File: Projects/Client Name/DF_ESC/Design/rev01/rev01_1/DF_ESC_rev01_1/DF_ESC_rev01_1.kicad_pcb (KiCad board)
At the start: 2 copper layers, 100 x 75 mm, 186 parts, among them J1 XT60PW-M, J2 HX25003-8AWB, J3 S6B-XH-SM4-TB(LF)(SN), J4 XH-3AWB, J5 7461084, J6 7461084, J7 7461084, J8 USB_C_Receptacle_USB2.0, Q1 HSBA15810C, Q2 HSBA15810C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

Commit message: Update 20240416
Lesson 16 finished
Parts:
- added R64: 2k2, Resistor_SMD:R_0603_1608Metric_Pad0.98x0.95mm_HandSolder, F.Cu at (210.7, 131.1)
- C39, C42, C46: moved to B.Cu
- C41, C43, C45: footprint Capacitor_SMD:C_0603_1608Metric_Pad1.08x0.95mm_HandSolder -> Capacitor_SMD:C_1210_3225Metric
- D7: footprint PESD3V3U1UA:SOD-323_L1.7-W1.3-LS2.5-RD -> Diode_SMD:D_SOD-323_HandSoldering
- D9: footprint Diode_SMD:D_SOD-323 -> Diode_SMD:D_SOD-323_HandSoldering
- moved TH1 105.4 mm to (199.1, 156.3)
- moved R1 103.7 mm to (199.1, 157.9), turned to 180 degrees
- moved C3 100.2 mm to (201.7, 157.1), turned to 90 degrees
- moved C23 35.8 mm to (206.7, 106.3), turned to 90 degrees
- moved R20 35.2 mm to (274.4, 129.4), turned to 180 degrees
- moved D12 34.5 mm to (239.9, 167.4), turned to 90 degrees
- moved R13 33.4 mm to (205.1, 106.3), turned to 90 degrees
- moved D11 32.5 mm to (237.3, 167.4), turned to 90 degrees
- moved R21 31.7 mm to (274.5, 130.9), turned to 180 degrees
- moved R58 31.1 mm to (223.4, 128.9)
- moved R59 31.1 mm to (224.9, 128.9)
- moved R24 30.8 mm to (274.4, 159.3), turned to 180 degrees
- moved R25 28.7 mm to (274.4, 160.8), turned to 180 degrees
- moved R22 27.7 mm to (274.4, 144.3), turned to 180 degrees
- moved R11 27.1 mm to (239.9, 163.1), turned to -90 degrees
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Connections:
- C57 pad 1: +5V -> +3V3
- C58 pad 1: +5V -> +3V3
- C59 pad 1: +5V -> +3V3
- C60 pad 1: +5V -> +3V3
- R45 pad 1: +5V -> +3V3
- R46 pad 1: +5V -> +3V3
- R47 pad 1: +5V -> +3V3
- R48 pad 1: +5V -> +3V3
- SW1 pad 1: GND -> Net-(R64-Pad1)
- U6 pad 1: /[7] - CAN/C_CAN_P -> /[7] - CAN/C_CAN_N
- U6 pad 2: /[7] - CAN/C_CAN_N -> /[7] - CAN/C_CAN_P
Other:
- copper layers 2 -> 4

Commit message: update 2024-04-18
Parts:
- moved R28 12.5 mm to (251.9, 150.1), turned to 0 degrees
- moved C49 11.0 mm to (249.4, 153.4), turned to 90 degrees
- moved C48 10.6 mm to (249.2, 149.2), turned to 90 degrees
- moved R34 9.13 mm to (252.0, 154.2), turned to 0 degrees
- moved R29 8.34 mm to (251.9, 148.3), turned to 0 degrees
- moved R58 7.84 mm to (229.2, 134.1)
- moved R35 5.99 mm to (252.0, 152.4), turned to 0 degrees
- moved R59 5.81 mm to (227.4, 134.1)
- moved C33 5.06 mm to (242.2, 155.7)
- moved C35 5.06 mm to (243.7, 155.7)
- moved C32 5.04 mm to (245.3, 155.7)
- moved C11 4.64 mm to (223.4, 133.6)
- moved C24 4.58 mm to (234.1, 150.8)
- moved C27 4.58 mm to (234.1, 152.3)
- moved C31 4.58 mm to (234.1, 153.8)
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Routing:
- net /[9] - USB/USB-C_P: track 0.00 -> 34.6 mm
- net /[9] - USB/USB-C_N: track 0.00 -> 33.9 mm
- net /[7] - CAN/C_CAN_P: track 0.00 -> 12.1 mm
- net /[7] - CAN/C_CAN_N: track 0.00 -> 11.9 mm
- net USB_N: track 0.00 -> 8.07 mm
- net USB_P: track 0.00 -> 6.77 mm
- net S2_P: track 0.00 -> 6.03 mm, vias 0 -> 1
- net S2_N: track 0.00 -> 4.82 mm, vias 0 -> 1
- net /[7] - CAN/CAN_P: track 0.00 -> 3.01 mm
- net /[7] - CAN/CAN_N: track 0.00 -> 3.01 mm
- net /[7] - CAN/R_CAN_P: track 0.00 -> 1.94 mm
- net /[7] - CAN/R_CAN_N: track 0.00 -> 1.94 mm
- net GND: vias 0 -> 2

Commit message: update 20240419
preliminari Routing
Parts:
- moved R35 12.0 mm to (257.8, 162.9)
- moved R29 11.9 mm to (257.6, 158.7)
- moved C49 10.4 mm to (255.3, 162.0), turned to -90 degrees
- moved C48 10.4 mm to (255.0, 157.8), turned to -90 degrees
- moved R34 9.04 mm to (257.8, 161.1)
- moved R28 8.94 mm to (257.6, 156.9)
- moved R31 8.20 mm to (258.6, 127.3)
- moved R37 8.20 mm to (258.6, 142.3)
- moved D14 8.20 mm to (250.8, 127.6)
- moved NT5 8.20 mm to (253.4, 142.7)
- moved NT8 8.20 mm to (253.4, 127.1)
- moved C46 2.59 mm to (245.2, 149.9)
- moved C42 2.57 mm to (245.2, 146.5)
- moved C39 2.56 mm to (245.2, 143.1)
- moved R17 2.06 mm to (249.8, 142.9)
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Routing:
- net S1_P: track 0.00 -> 28.8 mm, vias 0 -> 1
- net S1_N: track 0.00 -> 27.7 mm, vias 0 -> 1
- net M_L3: track 0.00 -> 25.5 mm
- net S2_N: track 4.82 -> 23.5 mm
- net H3_LOW: track 0.00 -> 18.1 mm
- net S2_P: track 6.03 -> 21.8 mm
- net M_H3: track 0.00 -> 14.9 mm
- net M_L2: track 0.00 -> 9.32 mm
- net H2_LOW: track 0.00 -> 9.11 mm
- net M_H2: track 0.00 -> 8.92 mm
- net +VDC: track 0.00 -> 8.83 mm, vias 0 -> 30
- net H1_LOW: track 0.00 -> 6.64 mm
- net /[6] - MOSFETs/SH2_N: track 0.00 -> 6.34 mm
- net /[6] - MOSFETs/SH1_P: track 0.00 -> 6.33 mm
- net M_L1: track 0.00 -> 6.08 mm
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- added copper zone on B.Cu, net +VDC
- added copper zone on F.Cu, net +VDC

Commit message: update 20240421
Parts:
- C26, C29, C30, R14: moved to B.Cu
- moved C26 9.57 mm to (243.0, 141.1), turned to -90 degrees
- moved R14 7.58 mm to (241.4, 141.1), turned to 90 degrees
- moved R19 6.69 mm to (233.2, 141.5), turned to 180 degrees
- moved C30 6.36 mm to (237.8, 146.5)
- moved C24 6.05 mm to (233.2, 144.8)
- moved R18 6.03 mm to (233.2, 139.9), turned to 0 degrees
- moved C27 5.97 mm to (233.2, 146.4)
- moved C29 5.74 mm to (239.8, 141.1), turned to 90 degrees
- moved R15 3.08 mm to (233.2, 143.1)
- moved R16 2.03 mm to (235.8, 138.9), turned to -90 degrees
- moved C25 0.95 mm to (233.2, 149.5)
- moved C28 0.95 mm to (233.2, 148.0)
- turned R21 to 0 degrees
- turned R23 to 0 degrees
- turned R25 to 0 degrees
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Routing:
- net H3_VS: track 1.98 -> 72.6 mm, vias 1 -> 3
- net H1_VS: track 1.87 -> 51.8 mm, vias 1 -> 2
- net H2_VS: track 1.49 -> 41.1 mm, vias 1 -> 4
- net /[4] - MCU/LED_RED: track 0.00 -> 36.8 mm, vias 0 -> 2
- net /[4] - MCU/LED_GREEN: track 0.00 -> 33.0 mm, vias 0 -> 2
- net H2: track 0.00 -> 30.6 mm, vias 0 -> 2
- net ADC_TEMP: track 0.00 -> 28.4 mm
- net BR_S02: track 0.00 -> 28.2 mm
- net H3: track 0.00 -> 27.5 mm
- net BR_S01: track 0.00 -> 27.3 mm
- net EN_GATE: track 0.00 -> 26.4 mm, vias 0 -> 2
- net H1: track 0.00 -> 26.0 mm, vias 0 -> 2
- net FAULT: track 0.00 -> 25.7 mm, vias 0 -> 2
- net /[4] - MCU/MISO_ADC_EXT2: track 0.00 -> 25.0 mm, vias 0 -> 2
- net L1: track 0.00 -> 24.7 mm, vias 0 -> 2
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
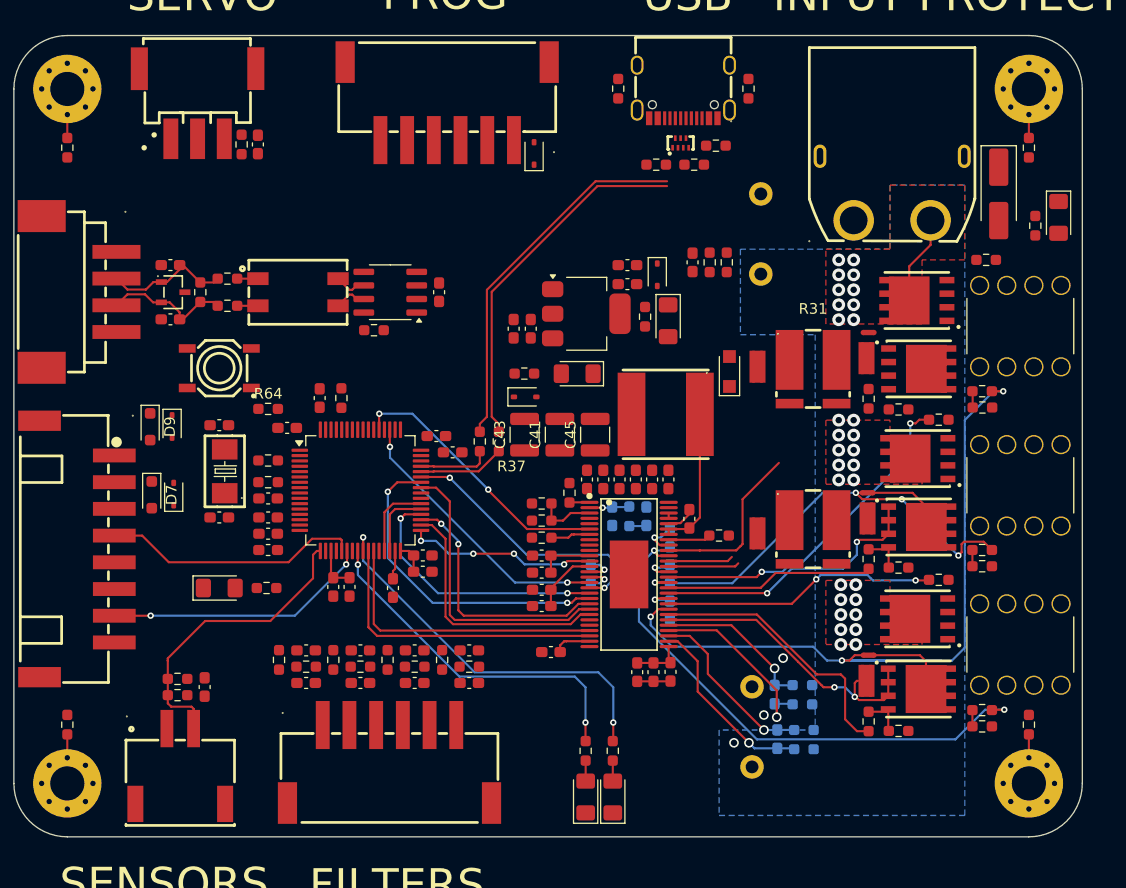
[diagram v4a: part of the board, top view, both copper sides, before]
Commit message: Update DF_ESC_rev01_1.kicad_pcb
Layout preliminar finished
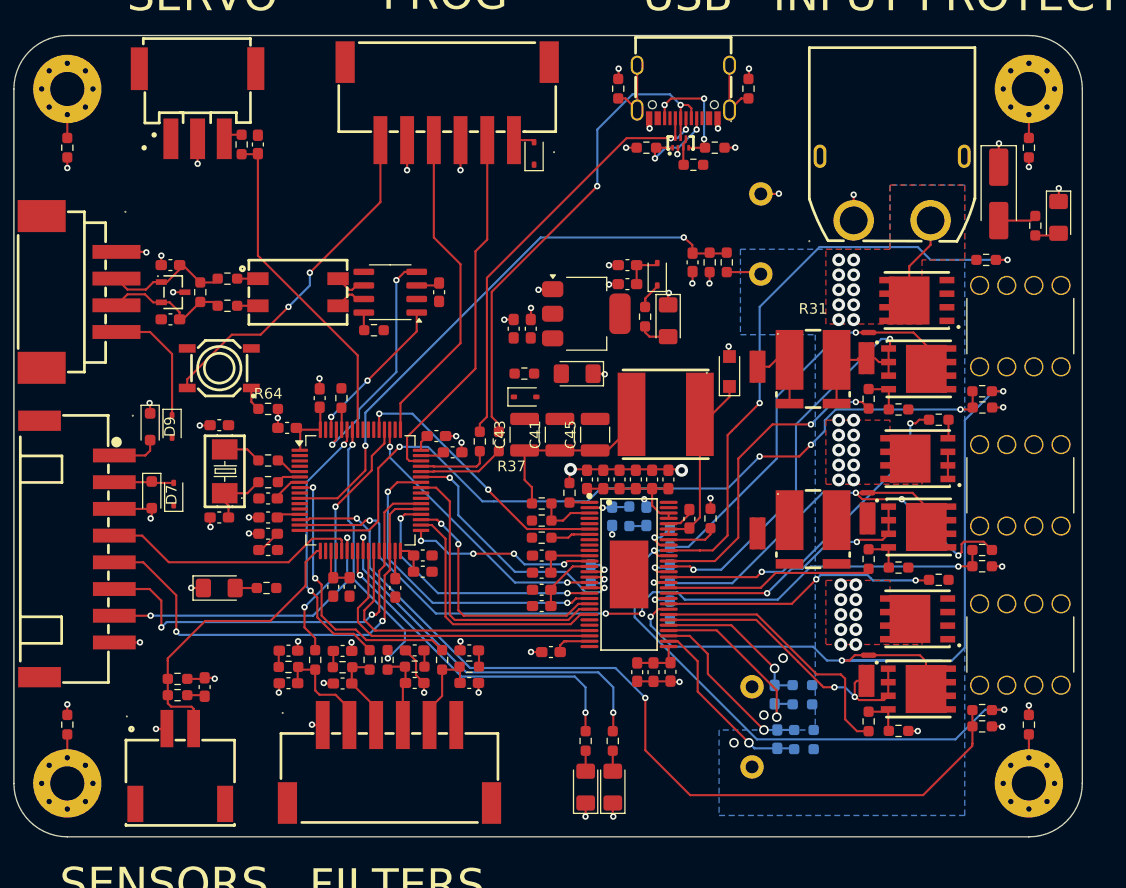
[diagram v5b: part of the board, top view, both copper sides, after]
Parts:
- moved R57 6.51 mm to (243.0, 106.6), turned to 180 degrees
- moved R56 5.71 mm to (249.4, 106.6), turned to 0 degrees
- moved R50 3.41 mm to (217.1, 154.6)
- moved R51 3.39 mm to (212.0, 154.6)
- moved R17 1.79 mm to (249.0, 141.3), turned to 90 degrees
- moved C54 1.67 mm to (214.6, 156.8)
- moved C58 1.67 mm to (214.6, 153.7)
- moved R46 1.67 mm to (214.6, 155.2)
- moved C55 1.65 mm to (209.5, 156.7)
- moved C59 1.65 mm to (209.5, 153.7)
- moved R47 1.65 mm to (209.5, 155.2)
- moved D11 0.93 mm to (237.3, 166.5)
- moved D12 0.93 mm to (239.9, 166.5)
- moved R10 0.93 mm to (237.3, 162.1)
- moved R11 0.93 mm to (239.9, 162.1)
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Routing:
- net GND: track 3.13 -> 101.3 mm, vias 3 -> 69
- net SENS3: track 1.52 -> 83.9 mm, vias 0 -> 2
- net SENS1: track 1.53 -> 77.1 mm, vias 0 -> 4
- net SENS2: track 1.52 -> 73.6 mm, vias 0 -> 4
- net AN_IN: track 0.00 -> 49.3 mm, vias 0 -> 2
- net M_H1: track 16.2 -> 55.8 mm, vias 0 -> 2
- net /[4] - MCU/TX_SDA_NSS: track 6.56 -> 43.8 mm, vias 0 -> 2
- net /[4] - MCU/NRST: track 0.00 -> 35.1 mm, vias 0 -> 2
- net /[4] - MCU/RX_SCL_MOSI: track 7.38 -> 42.0 mm, vias 0 -> 2
- net /[4] - MCU/SWDIO: track 0.00 -> 34.3 mm
- net H1_LOW: track 6.64 -> 38.6 mm, vias 0 -> 2
- net /[4] - MCU/SERVO: track 0.00 -> 31.2 mm
- net /[4] - MCU/SWCLK: track 0.00 -> 30.5 mm
- net H1_VS: track 51.8 -> 81.9 mm, vias 2 -> 3
- net TEMP_MOTOR: track 0.00 -> 26.2 mm, vias 0 -> 2
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
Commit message: update 20240423
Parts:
- moved NT4 13.6 mm to (275.2, 146.1), turned to -90 degrees
- moved NT1 9.18 mm to (269.5, 131.1), turned to -90 degrees
- moved R24 8.32 mm to (268.1, 164.6)
- moved R25 8.32 mm to (268.1, 166.1)
- moved R63 7.78 mm to (273.3, 166.1), turned to 180 degrees
- moved C48 5.91 mm to (250.2, 154.4)
- moved C49 5.91 mm to (250.4, 158.6)
- moved R29 5.91 mm to (252.8, 155.3)
- moved R28 5.91 mm to (252.8, 153.5)
- moved R34 5.91 mm to (252.9, 157.7)
- moved R35 5.91 mm to (252.9, 159.5)
- moved NT7 4.74 mm to (261.8, 158.4)
- moved Q5 4.22 mm to (268.8, 154.9)
- moved R39 4.22 mm to (270.8, 151.3)
- moved C1 4.01 mm to (257.0, 162.8)
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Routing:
- net H3_VS: track 72.6 -> 50.2 mm, vias 3 -> 2
- net S2_P: track 17.6 -> 0.84 mm
- net S2_N: track 16.5 -> 1.97 mm
- net S1_P: track 18.0 -> 4.50 mm
- net +VDC: track 31.4 -> 19.9 mm, vias 30 -> 31
- net H3_LOW: track 28.1 -> 16.9 mm, vias 2 -> 1
- net SENS3: track 83.9 -> 74.0 mm
- net /[5] - MOSFET DRIVER/+5V_DRV: track 17.3 -> 26.9 mm
- net H1_VS: track 81.9 -> 91.3 mm
- net S1_N: track 14.9 -> 5.87 mm
- net /[6] - MOSFETs/PHASE_1: track 7.60 -> 3.40 mm
- net /[6] - MOSFETs/PHASE_2: track 9.98 -> 6.05 mm
- net /[6] - MOSFETs/M_H1_RG: track 0.00 -> 3.89 mm
- net H2_LOW: track 25.5 -> 29.4 mm
- net Net-(Q6-G): track 3.97 -> 0.38 mm
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- added copper zone on F.Cu, net /[5] - MOSFET DRIVER/+5V_DRV

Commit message: update 20240423_2
Layout rehecho y terminado en casa falta solo mejorarlo
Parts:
- moved NT7 4.10 mm to (265.9, 158.2)
- moved NT2 0.44 mm to (263.9, 160.6), turned to 0 degrees
- moved Q6 0.44 mm to (268.8, 161.3)
- moved R24 0.44 mm to (268.1, 165.1)
- moved R25 0.44 mm to (268.1, 166.6)
- moved R38 0.44 mm to (262.7, 164.4)
- moved R40 0.44 mm to (264.3, 164.4)
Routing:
- net /[6] - MOSFETs/SH1_N: track 4.09 -> 35.6 mm, vias 0 -> 1
- net /[6] - MOSFETs/SH1_P: track 5.35 -> 36.7 mm, vias 0 -> 1
- net H3_VS: track 50.2 -> 77.3 mm, vias 2 -> 3
- net /[6] - MOSFETs/SH2_P: track 0.00 -> 20.3 mm, vias 0 -> 3
- net /[6] - MOSFETs/SH2_N: track 0.00 -> 19.0 mm, vias 0 -> 1
- net H3_LOW: track 16.9 -> 30.6 mm, vias 1 -> 2
- net S2_P: track 0.84 -> 11.8 mm
- net S2_N: track 1.97 -> 10.5 mm
- net /[6] - MOSFETs/PHASE_3: track 9.70 -> 4.37 mm
- net S1_P: track 4.50 -> 8.72 mm
- net S1_N: track 5.87 -> 7.71 mm
- net M_L3: track 28.5 -> 27.2 mm

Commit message: update 20240424
Layout mejorado y terminado. Dar un ultimo repaso
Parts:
- moved C15 1.35 mm to (211.6, 131.1), turned to 180 degrees
- moved J1 0.81 mm to (265.9, 105.5)
- moved C53 0.61 mm to (221.3, 157.3)
- moved C54 0.61 mm to (214.6, 157.4)
- moved C55 0.61 mm to (209.5, 157.3)
- moved C56 0.61 mm to (226.4, 157.3)
- moved C57 0.61 mm to (221.3, 154.3)
- moved C58 0.61 mm to (214.6, 154.3)
- moved C59 0.61 mm to (209.5, 154.3)
- moved C60 0.61 mm to (226.4, 154.3)
- moved R45 0.61 mm to (221.3, 155.8)
- moved R46 0.61 mm to (214.6, 155.8)
- moved R47 0.61 mm to (209.5, 155.8)
- moved R48 0.61 mm to (226.4, 155.8)
- moved R49 0.61 mm to (218.8, 155.2)
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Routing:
- net +3V3: track 27.8 -> 289.6 mm, vias 0 -> 18
- net +5V: track 11.8 -> 200.5 mm, vias 0 -> 4
- net +VDC: track 19.9 -> 92.4 mm, vias 31 -> 32
- net GND: track 99.6 -> 130.3 mm, vias 69 -> 83
- net /[5] - MOSFET DRIVER/DVDD: track 5.21 -> 18.7 mm, vias 0 -> 2
- net /[3] - STEP DOWN/+3V3_IC: track 3.79 -> 13.5 mm
- net /[6] - MOSFETs/M_H3_RG: track 0.00 -> 1.78 mm
- net Net-(Q6-G): track 0.38 -> 2.14 mm
- net M_H1: track 58.5 -> 57.1 mm
- net HALL_1_OUT: track 25.4 -> 24.1 mm
- net TEMP_MOTOR: track 26.2 -> 27.4 mm
- net SENS2: track 74.4 -> 75.5 mm
- net /[9] - USB/USB-C_P: track 42.8 -> 43.9 mm
- net /[6] - MOSFETs/PHASE_3: track 4.37 -> 5.48 mm
- net BR_S02: track 29.3 -> 28.2 mm
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- added copper zone on F.Cu, net +3V3
- added copper zone on B.Cu, net +5V
- added copper zone on F.Cu, net /[6] - MOSFETs/PHASE_1
- added copper zone on F.Cu, net /[6] - MOSFETs/PHASE_2
- added copper zone on F.Cu, net /[6] - MOSFETs/PHASE_3
- added copper zone on F.Cu, net /[6] - MOSFETs/SH1_N
- added copper zone on F.Cu, net /[6] - MOSFETs/SH1_P
- added copper zone on F.Cu, net /[6] - MOSFETs/SH2_N
- added copper zone on F.Cu, net /[6] - MOSFETs/SH2_P
- added copper zone on In1.Cu, net GND
- added copper zone on In2.Cu, net GND
- added copper zone on F.Cu, net H1_LOW
- added copper zone on F.Cu, net H2_LOW
- added copper zone on F.Cu, net H3_LOW
